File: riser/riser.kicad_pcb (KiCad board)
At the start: 2 copper layers, 140.8 x 95 mm, 3 parts, among them J1 DIN41612_02x32_AB, J2 DIN41612_02x32_AB

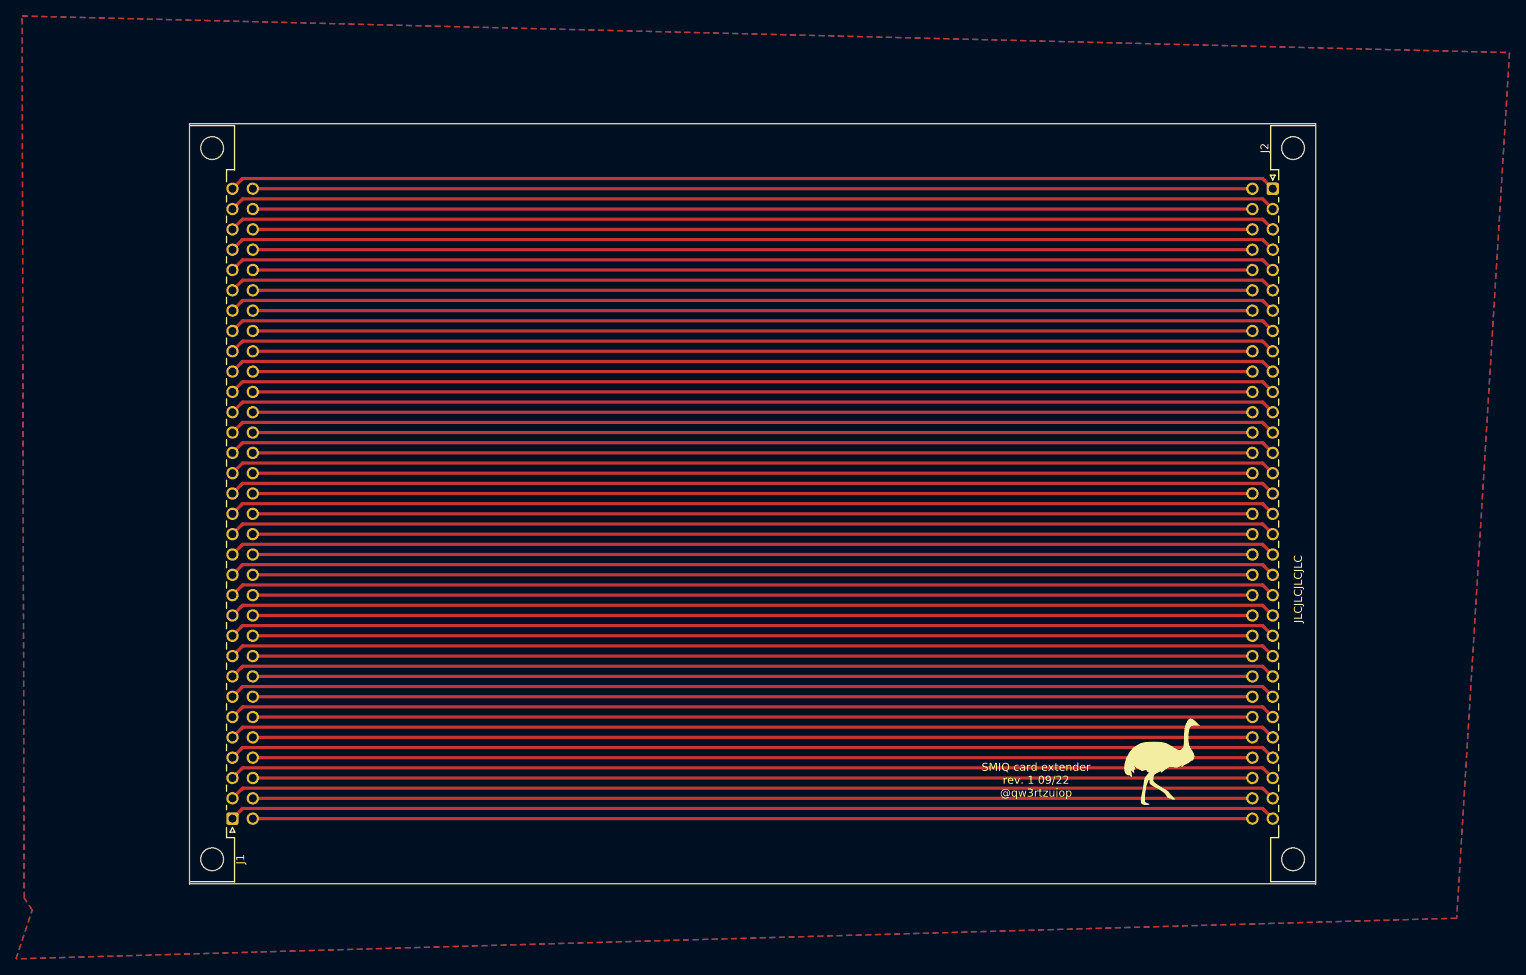
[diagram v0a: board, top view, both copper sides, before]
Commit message: smiq modules silkscreen added
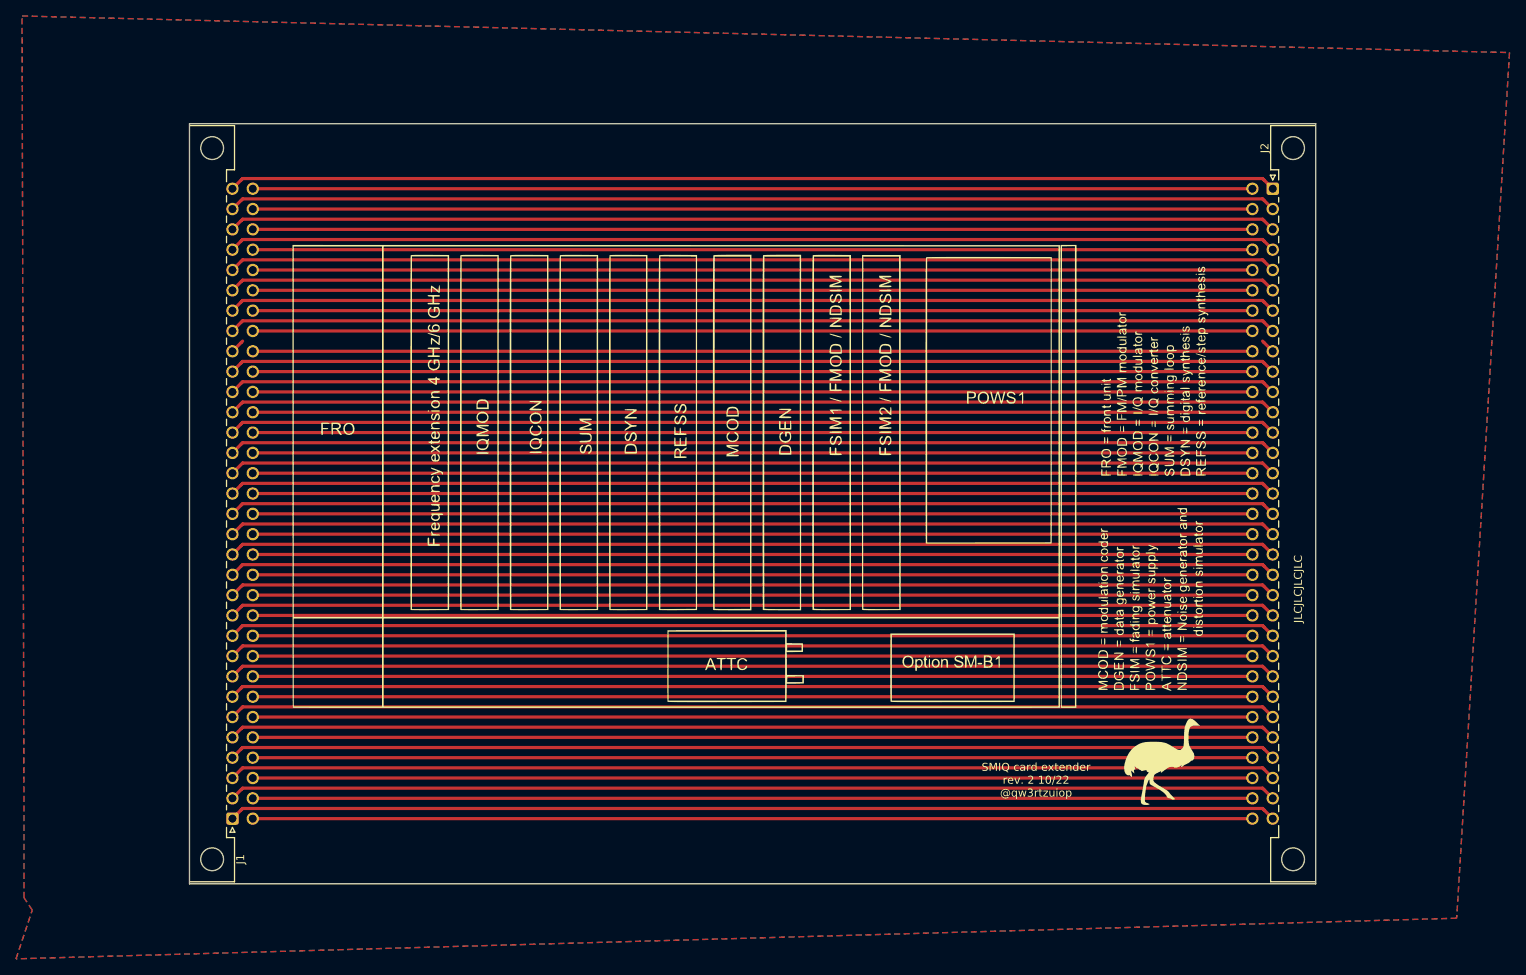
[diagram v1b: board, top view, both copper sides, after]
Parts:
- added G***: LOGO, LOGO, F.Cu at (131.8, 108.0)
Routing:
- net Net-(J2-Pada9): track 131.1 -> 3.59 mm
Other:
- board text added: "SMIQ card extender rev. 2 10/22 @qw3rtzuiop"
- board text removed: "SMIQ card extender rev. 1 09/22 @qw3rtzuiop"
